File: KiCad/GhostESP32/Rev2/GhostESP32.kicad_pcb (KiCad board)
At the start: 2 copper layers, 60 x 37 mm, 33 parts, among them J1 CONN_02X20, P1 USB_OTG, Q1 Q_NPN_BEC, Q2 Q_NPN_BEC, SW1 SW_SPDT, U1 LM358, U2 NCP1117ST33T3G, U3 CP2102, U4 ESP-WROOM-32

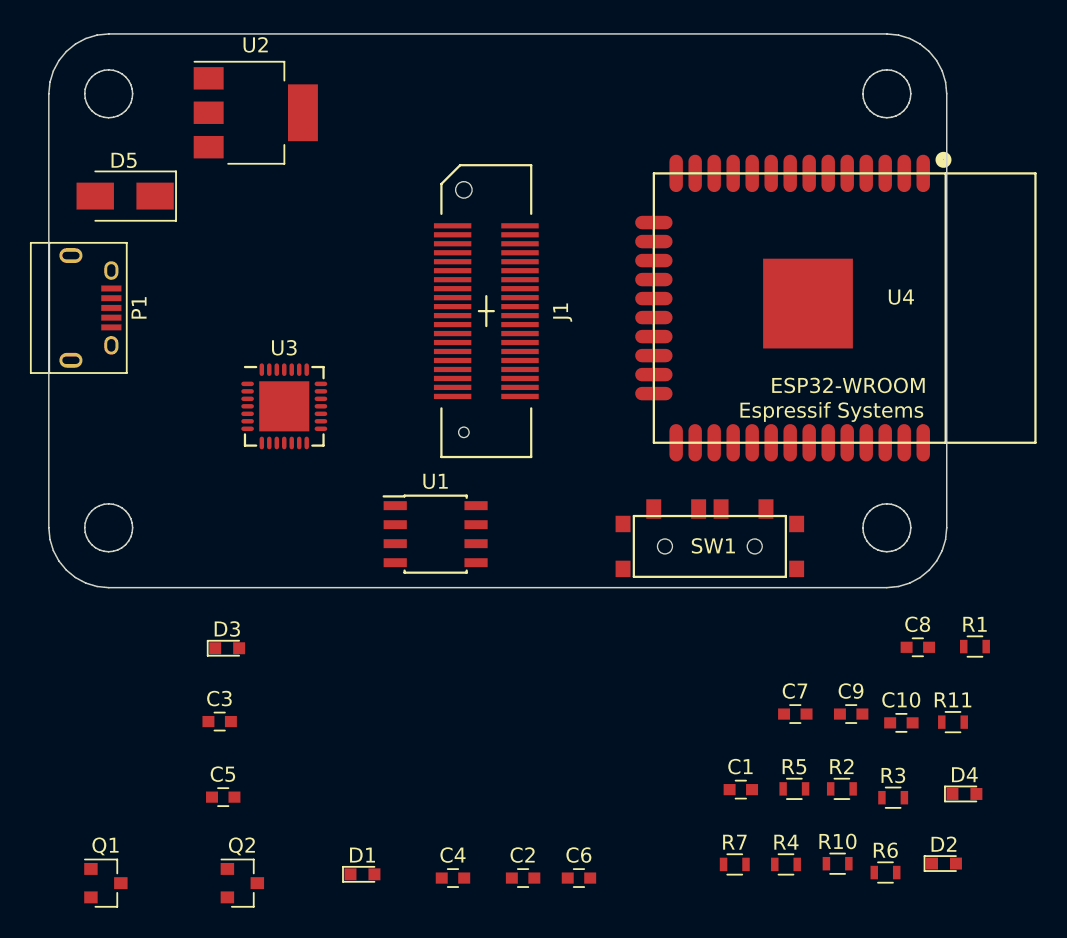
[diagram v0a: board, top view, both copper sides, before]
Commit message: Made a connectorboard
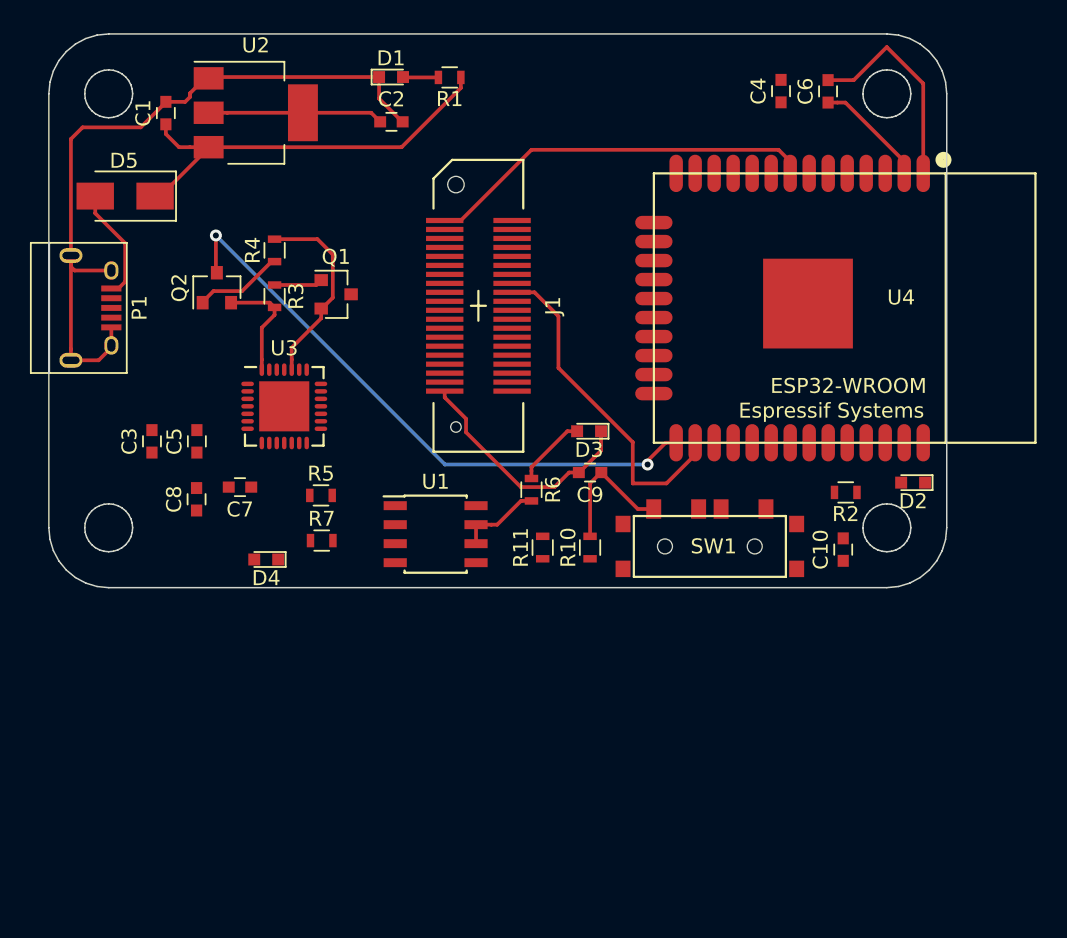
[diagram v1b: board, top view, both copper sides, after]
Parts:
- moved C1 59.3 mm to (124.8, 76.0), turned to 90 degrees
- moved C4 57.0 mm to (165.9, 74.5), turned to 90 degrees
- moved C6 55.1 mm to (169.0, 74.6), turned to 90 degrees
- moved R4 53.4 mm to (132.0, 85.2), turned to 90 degrees
- moved D1 53.3 mm to (139.8, 73.6)
- moved R3 53.2 mm to (132.0, 88.2), turned to 270 degrees
- moved R1 51.8 mm to (143.7, 73.6), turned to 180 degrees
- moved C2 51.3 mm to (139.9, 76.6)
- moved D4 49.2 mm to (131.5, 105.8), turned to 180 degrees
- moved C8 49.2 mm to (126.8, 101.8), turned to 90 degrees
- moved Q1 42.2 mm to (136.2, 88.1)
- moved C7 40.1 mm to (129.7, 101.0), turned to 180 degrees
- moved Q2 39.8 mm to (128.2, 87.7), turned to 90 degrees
- moved R5 37.2 mm to (135.2, 101.6)
- moved R7 35.1 mm to (135.2, 104.6)
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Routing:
- net GND: track 0.00 -> 79.3 mm
- net IO0: track 0.00 -> 40.4 mm, vias 0 -> 2
- net +5V: track 0.00 -> 28.0 mm
- net IO32: track 0.00 -> 26.2 mm
- net IO4: track 0.80 -> 22.8 mm
- net +3V3: track 0.00 -> 19.2 mm
- net RTS: track 0.00 -> 13.2 mm
- net Net-(C9-Pad1): track 0.00 -> 9.10 mm
- net Net-(D5-Pad2): track 0.00 -> 7.66 mm
- net DTR: track 0.00 -> 7.55 mm
- net Net-(Q2-Pad1): track 0.00 -> 5.97 mm
- net Net-(R6-Pad2): track 0.00 -> 5.63 mm
- net Net-(D3-Pad2): track 0.00 -> 4.80 mm
- net Net-(Q1-Pad1): track 0.00 -> 3.25 mm
- net Net-(D1-Pad2): track 0.00 -> 2.38 mm

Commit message: Working on the Encoder
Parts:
- added C11: 0.1uF, Capacitors_SMD:C_0603, F.Cu at (139.1, 93.1)
- added C12: 10nF, Capacitors_SMD:C_0603, F.Cu at (140.7, 81.3)
- added C13: 2.2nF, Capacitors_SMD:C_0603, F.Cu at (137.2, 81.2)
- added C14: 0.22uF, Capacitors_SMD:C_0603, F.Cu at (157.4, 73.4)
- added C15: 4.7uF, Capacitors_SMD:C_0603, F.Cu at (161.0, 73.3)
- added R8: 2k2, Resistors_SMD:R_0603, F.Cu at (147.1, 73.6)
- added R9: 2k2, Resistors_SMD:R_0603, F.Cu at (147.1, 76.3)
- added U5: MPU-6050, Housings_DFN_QFN:QFN-24-1EP_4x4mm_Pitch0.5mm, F.Cu at (138.1, 86.8)
- added U6: HMC5883, Housings_DFN_QFN:QFN-16-1EP_3x3mm_Pitch0.5mm, F.Cu at (152.1, 75.1)
- moved Q1 4.96 mm to (131.7, 86.0)
- moved R4 4.16 mm to (128.9, 82.5), turned to 0 degrees
- moved R3 3.48 mm to (128.8, 89.6), turned to 180 degrees
- moved Q2 2.56 mm to (126.2, 86.1)
- moved D3 2.36 mm to (152.6, 99.6)
- moved J1 1.93 mm to (147.6, 88.8)
- moved C9 1.70 mm to (152.5, 101.6)
- moved R6 0.78 mm to (148.7, 101.8)
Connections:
- J1 pad 1: IO32 -> IO27
- J1 pad 11: Net-(J1-Pad11) -> (no net)
- J1 pad 12: Net-(J1-Pad12) -> (no net)
- J1 pad 13: Net-(J1-Pad13) -> (no net)
- J1 pad 14: Net-(J1-Pad14) -> (no net)
- J1 pad 21: Net-(J1-Pad21) -> IO23
- J1 pad 22: Net-(J1-Pad22) -> IO22
- J1 pad 23: Net-(J1-Pad23) -> IO21
- J1 pad 24: Net-(J1-Pad24) -> IO19
- J1 pad 25: Net-(J1-Pad25) -> IO18
- J1 pad 26: Net-(J1-Pad26) -> IO17
- J1 pad 27: +5V -> IO16
- J1 pad 28: +5V -> IO4
- J1 pad 29: +5V -> (no net)
- J1 pad 3: IO33 -> IO25
- J1 pad 30: +5V -> (no net)
- J1 pad 31: Net-(J1-Pad31) -> (no net)
- J1 pad 32: IO4 -> (no net)
- J1 pad 33: IO17 -> IO13
- J1 pad 34: IO16 -> IO14
- J1 pad 35: IO19 -> +5V
- J1 pad 36: IO18 -> +5V
- J1 pad 37: IO22 -> +5V
- J1 pad 38: IO21 -> +5V
- J1 pad 39: IO13 -> +5V
- J1 pad 4: IO27 -> IO33
- J1 pad 40: IO23 -> +5V
- J1 pad 5: IO25 -> IO32
- J1 pad 6: IO14 -> (no net)
- P1 pad 4: Net-(P1-Pad4) -> (no net)
- SW1 pad 1: Net-(SW1-Pad1) -> (no net)
- U3 pad 1: Net-(U3-Pad1) -> (no net)
- U3 pad 10: Net-(U3-Pad10) -> (no net)
- U3 pad 11: Net-(U3-Pad11) -> (no net)
- U3 pad 12: Net-(U3-Pad12) -> (no net)
- U3 pad 13: Net-(U3-Pad13) -> (no net)
- U3 pad 14: Net-(U3-Pad14) -> (no net)
- U3 pad 15: Net-(U3-Pad15) -> (no net)
- U3 pad 16: Net-(U3-Pad16) -> (no net)
- U3 pad 17: Net-(U3-Pad17) -> (no net)
- U3 pad 18: Net-(U3-Pad18) -> (no net)
- U3 pad 19: Net-(U3-Pad19) -> (no net)
- U3 pad 2: Net-(U3-Pad2) -> (no net)
- U3 pad 20: Net-(U3-Pad20) -> (no net)
- U3 pad 21: Net-(U3-Pad21) -> (no net)
- U3 pad 22: Net-(U3-Pad22) -> (no net)
- U3 pad 23: Net-(U3-Pad23) -> (no net)
- U3 pad 27: Net-(U3-Pad27) -> (no net)
- U3 pad 9: Net-(U3-Pad9) -> (no net)
- U4 pad 17: Net-(U4-Pad17) -> (no net)
- U4 pad 18: Net-(U4-Pad18) -> (no net)
- U4 pad 19: Net-(U4-Pad19) -> (no net)
- U4 pad 20: Net-(U4-Pad20) -> (no net)
- U4 pad 21: Net-(U4-Pad21) -> (no net)
- U4 pad 22: Net-(U4-Pad22) -> (no net)
- U4 pad 23: IO15 -> (no net)
- U4 pad 24: Net-(U4-Pad24) -> (no net)
- U4 pad 29: IO5 -> (no net)
- U4 pad 32: Net-(U4-Pad32) -> (no net)
- U4 pad 4: SENSOR_VP -> (no net)
- U4 pad 5: SENSOR_VN -> (no net)
- U4 pad 6: IO34 -> (no net)
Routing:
- net +3V3: track 19.2 -> 93.6 mm, vias 0 -> 2
- net EN: track 0.00 -> 72.0 mm, vias 0 -> 3
- net TXD: track 0.00 -> 39.8 mm, vias 0 -> 2
- net IO23: track 0.00 -> 38.0 mm, vias 0 -> 2
- net IO35: track 0.00 -> 35.1 mm, vias 0 -> 2
- net RXD: track 0.00 -> 32.8 mm, vias 0 -> 2
- net IO33: track 0.00 -> 31.2 mm
- net IO22: track 0.00 -> 28.2 mm, vias 0 -> 2
- net IO25: track 0.00 -> 28.2 mm
- net GND: track 79.3 -> 52.0 mm
- net IO21: track 0.00 -> 27.0 mm
- net IO26: track 0.00 -> 25.2 mm
- net IO19: track 0.00 -> 24.3 mm
- net IO32: track 26.2 -> 49.8 mm, vias 0 -> 4
- net IO18: track 0.00 -> 22.9 mm
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
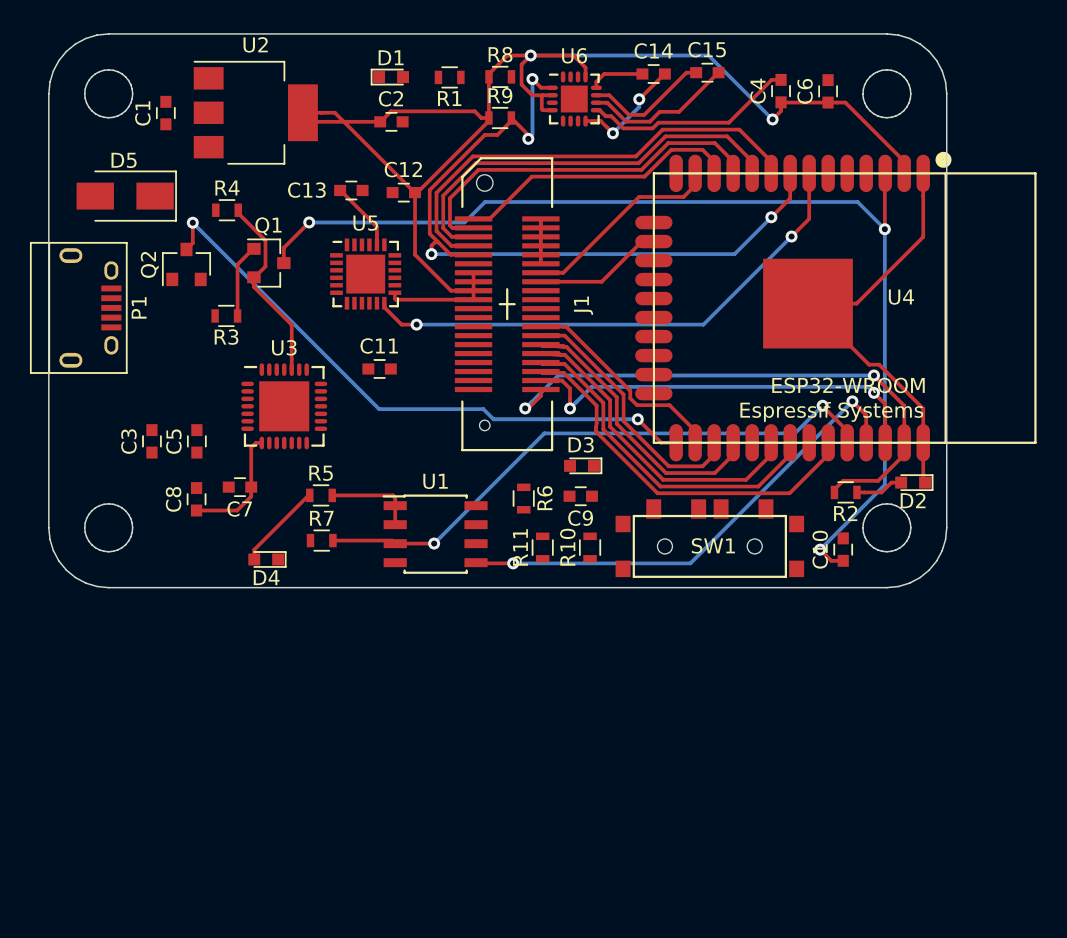
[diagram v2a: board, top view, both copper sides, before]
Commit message: Ready to start routing. Schematics should be done.
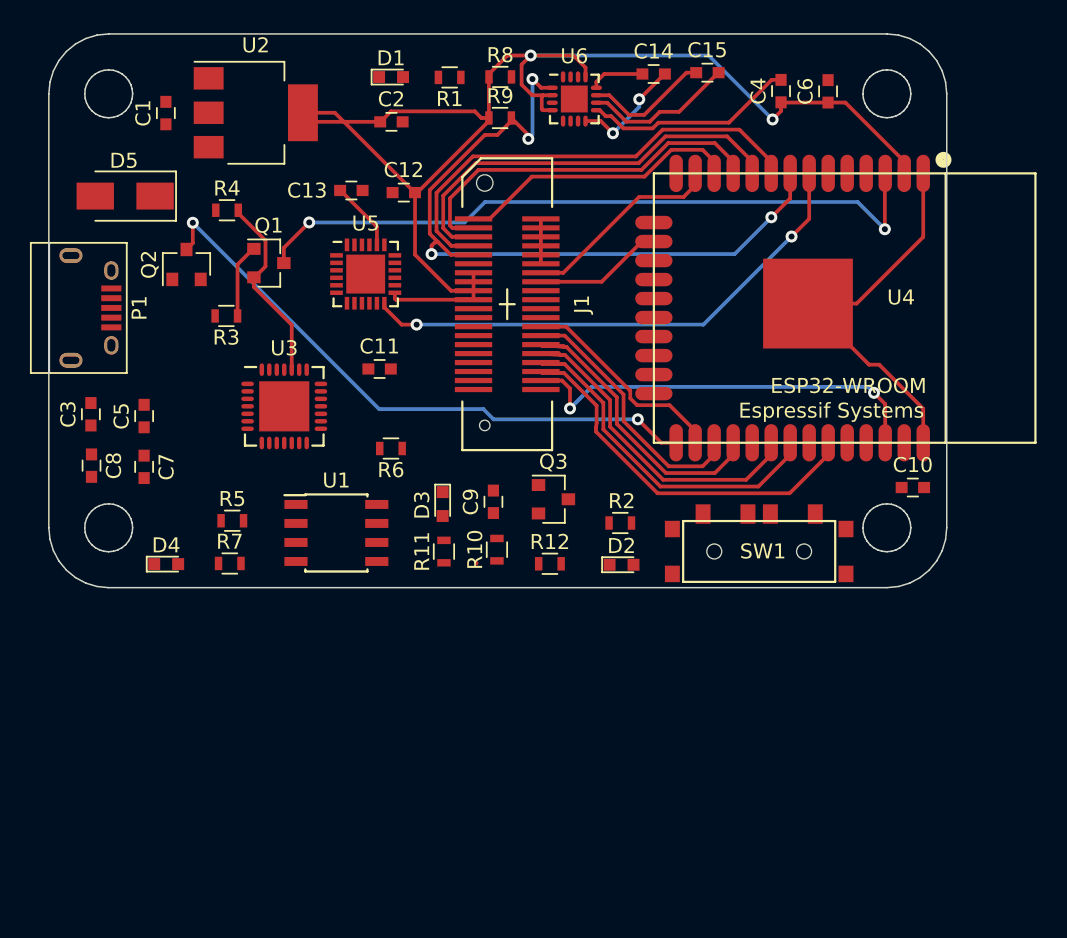
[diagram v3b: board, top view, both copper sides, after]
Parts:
- added Q3: Q_NPN_BEC, TO_SOT_Packages_SMD:SOT-23, F.Cu at (150.7, 101.8)
- added R12: 10k, Resistors_SMD:R_0603, F.Cu at (150.4, 106.1)
- moved D2 20.2 mm to (155.2, 106.2), turned to 0 degrees
- moved R2 15.2 mm to (155.2, 103.4)
- moved D3 9.66 mm to (143.3, 102.1), turned to 270 degrees
- moved R6 9.48 mm to (139.8, 98.4), turned to 180 degrees
- moved C8 7.37 mm to (119.8, 99.6), turned to 270 degrees
- moved D4 6.69 mm to (124.8, 106.1), turned to 0 degrees
- moved U1 6.63 mm to (136.2, 104.1)
- moved R11 6.60 mm to (143.4, 105.3)
- moved C7 6.55 mm to (123.3, 99.6), turned to 270 degrees
- moved R7 6.33 mm to (129.1, 106.1)
- moved C10 6.23 mm to (174.7, 101.0), turned to 0 degrees
- moved R10 6.22 mm to (146.9, 105.2)
- moved R5 6.16 mm to (129.2, 103.2)
- moved C9 5.85 mm to (146.7, 102.0), turned to 90 degrees
- moved C3 4.46 mm to (119.8, 96.1)
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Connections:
- D2 pad 1: GND -> LED
- J1 pad 13: (no net) -> GND
- J1 pad 14: (no net) -> GND
- J1 pad 21: IO23 -> LED
- R2 pad 2: IO23 -> +3V3
- U4 pad 14: IO12 -> (no net)
- U4 pad 6: (no net) -> IO34
- U5 pad 11: IO12 -> GND
- U6 pad 15: IO14 -> IO34
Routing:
- net TXD: track 39.8 -> 0.80 mm, vias 2 -> 0
- net IO23: track 38.0 -> 0.80 mm, vias 2 -> 0
- net RXD: track 32.8 -> 0.00 mm, vias 2 -> 0
- net EN: track 72.0 -> 46.9 mm, vias 3 -> 2
- net +5V: track 11.1 -> 3.00 mm
- net Net-(R5-Pad2): track 6.09 -> 0.00 mm
- net Net-(D4-Pad2): track 5.87 -> 0.00 mm
- net Net-(D2-Pad2): track 3.22 -> 0.00 mm
- net GND: track 52.0 -> 49.2 mm

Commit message: Ghost ESP32 done routing. Created Gerbers.
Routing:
- net GND: track 49.2 -> 321.5 mm, vias 0 -> 8
- net +3V3: track 93.6 -> 215.9 mm, vias 2 -> 10
- net +5V: track 3.00 -> 105.1 mm, vias 0 -> 4
- net RXD: track 0.00 -> 62.3 mm, vias 0 -> 3
- net EN: track 46.9 -> 109.0 mm, vias 2 -> 4
- net TXD: track 0.80 -> 45.7 mm, vias 0 -> 2
- net IO33: track 31.2 -> 71.3 mm, vias 0 -> 4
- net IO23: track 0.80 -> 29.5 mm
- net IO34: track 0.00 -> 22.7 mm, vias 0 -> 2
- net Net-(R7-Pad1): track 0.00 -> 20.0 mm, vias 0 -> 2
- net Net-(C9-Pad1): track 0.00 -> 16.8 mm, vias 0 -> 2
- net USB_DN: track 0.00 -> 15.8 mm, vias 0 -> 2
- net LED: track 0.00 -> 14.0 mm
- net USB_DP: track 0.00 -> 13.1 mm, vias 0 -> 2
- net DTR: track 0.00 -> 8.01 mm
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- added copper zone on B.Cu, net GND
- added copper zone on F.Cu, net GND
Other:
- board text added: "Ghost ESP32, rev 2 Frode Lillerud 19.mar 2017"
- board text added: "X"
- board text added: "Y"
